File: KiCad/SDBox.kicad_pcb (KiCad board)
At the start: 2 copper layers, 52.5 x 59 mm, 18 parts, among them J1 DB25_Male, J2 Micro_SD_Card_Socket, U1 Rapberry_Pi_Pico_2W, U2 SN74CB3T16210

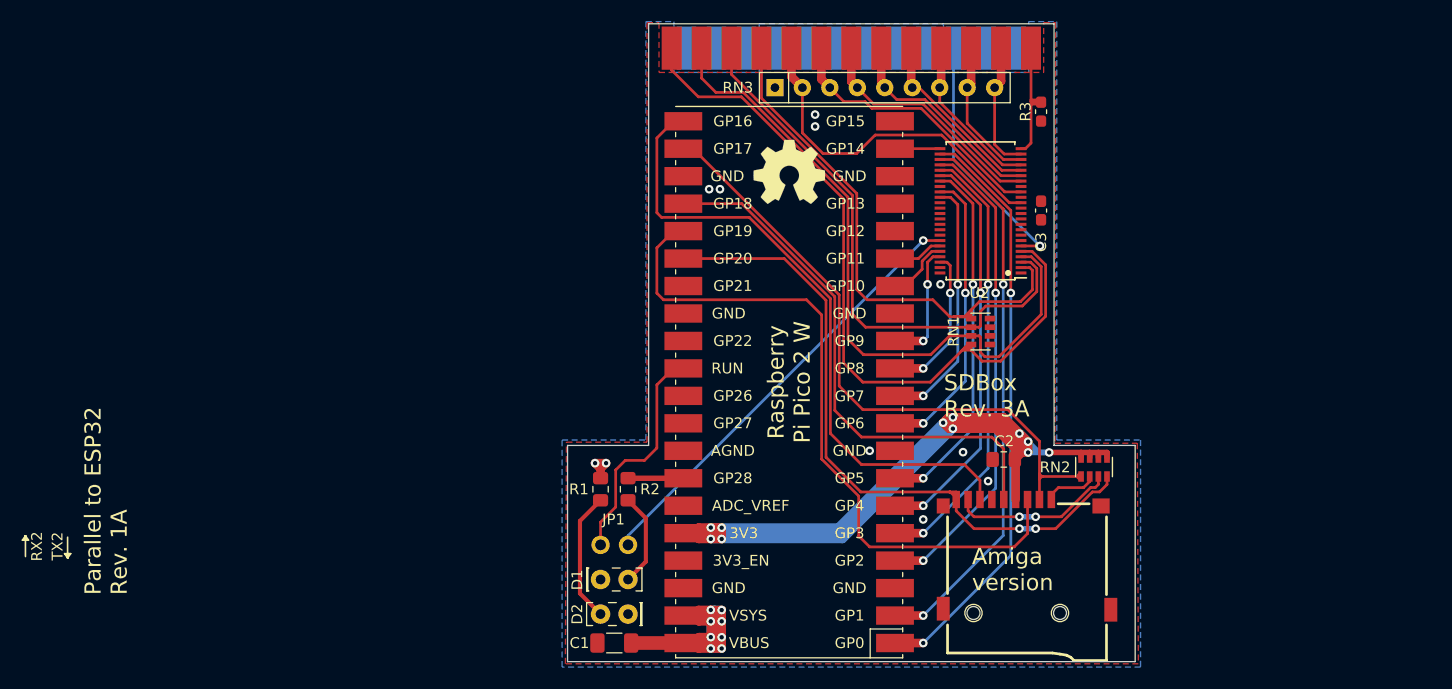
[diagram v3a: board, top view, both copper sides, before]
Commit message: Change board to four layer
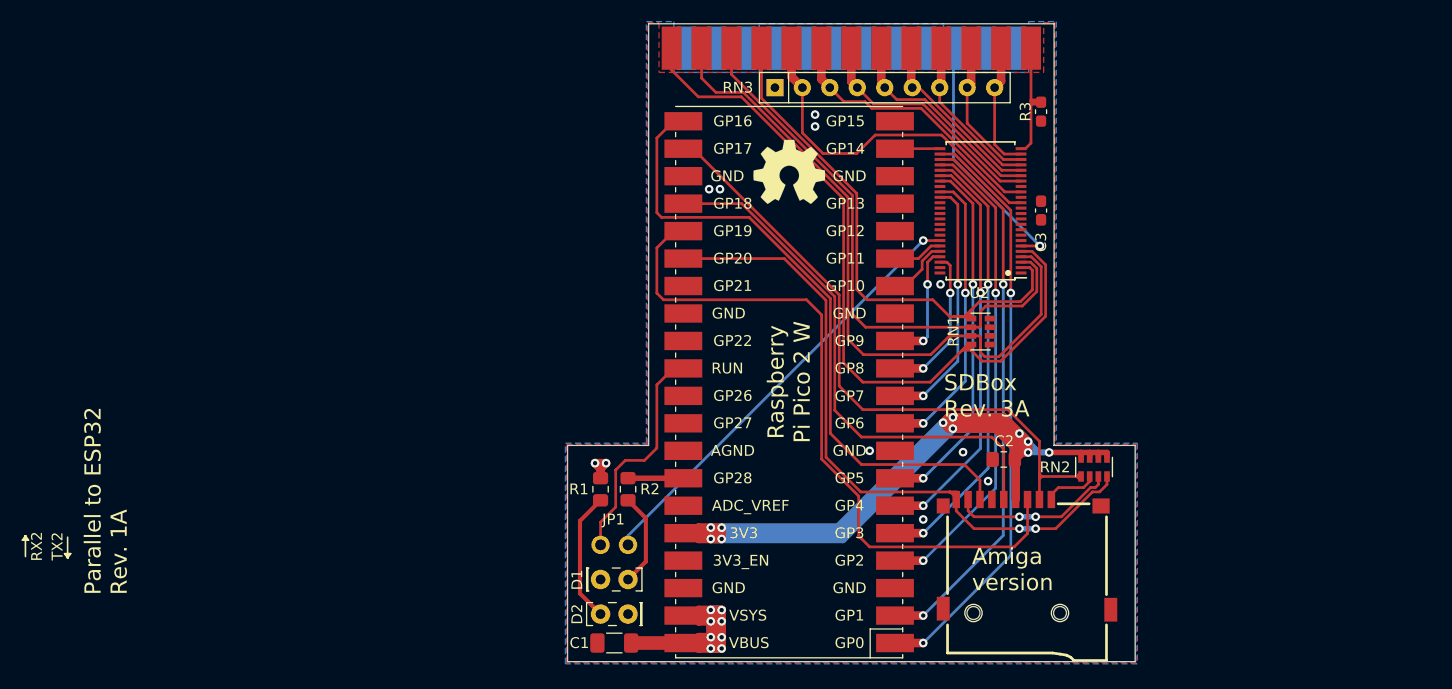
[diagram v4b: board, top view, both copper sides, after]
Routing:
- net VCC: track 49.1 -> 48.2 mm
- net GND: vias 7 -> 9
- net (no net): vias 2 -> 0
- added copper zone on GND, net GND
- added copper zone on VCC, net VCC
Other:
- copper layers 2 -> 4
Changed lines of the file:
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@@
   (general
     (thickness 1.6)
-    (drawings 39)
-    (tracks 481)
+    (drawings 34)
+    (tracks 479)
     (zones 0)
     (modules 18)
@@
   (layers
     (0 F.Cu signal)
+    (1 GND power)
+    (2 VCC power)
     (31 B.Cu signal)
     (32 B.Adhes user)
@@
     (arrow2b (pts (xy 131.45 153.5) (xy 132.576504 152.913579)))
   )
-  (dimension 7 (width 0.15) (layer Dwgs.User)
-    (gr_text "7.000 mm" (at 110.65 127.5 270) (layer Dwgs.User)
-      (effects (font (size 1 1) (thickness 0.15)))
-    )
-    (feature1 (pts (xy 166.45 131) (xy 111.363579 131)))
-    (feature2 (pts (xy 166.45 124) (xy 111.363579 124)))
-    (crossbar (pts (xy 111.95 124) (xy 111.95 131)))
-    (arrow1a (pts (xy 111.95 131) (xy 111.363579 129.873496)))
-    (arrow1b (pts (xy 111.95 131) (xy 112.536421 129.873496)))
-    (arrow2a (pts (xy 111.95 124) (xy 111.363579 125.126504)))
-    (arrow2b (pts (xy 111.95 124) (xy 112.536421 125.126504)))
-  )
-  (dimension 46 (width 0.15) (layer Dwgs.User)
-    (gr_text "46.000 mm" (at 177.75 108 270) (layer Dwgs.User)
-      (effects (font (size 1 1) (thickness 0.15)))
-    )
-    (feature1 (pts (xy 166.45 131) (xy 177.036421 131)))
-    (feature2 (pts (xy 166.45 85) (xy 177.036421 85)))
-    (crossbar (pts (xy 176.45 85) (xy 176.45 131)))
-    (arrow1a (pts (xy 176.45 131) (xy 175.863579 129.873496)))
-    (arrow1b (pts (xy 176.45 131) (xy 177.036421 129.873496)))
-    (arrow2a (pts (xy 176.45 85) (xy 175.863579 86.126504)))
-    (arrow2b (pts (xy 176.45 85) (xy 177.036421 86.126504)))
-  )
   (gr_line (start 121.45 144) (end 173.95 144) (layer Edge.Cuts) (width 0.05))
   (gr_line (start 121.45 124) (end 121.45 144) (layer Edge.Cuts) (width 0.05))
@@
   (gr_line (start 173.95 124) (end 173.95 144) (layer Edge.Cuts) (width 0.05))
   (gr_line (start 166.45 124) (end 173.95 124) (layer Edge.Cuts) (width 0.05))
-  (dimension 52.5 (width 0.15) (layer Dwgs.User)
-    (gr_text "52.500 mm" (at 147.7 145.05) (layer Dwgs.User)
-      (effects (font (size 1 1) (thickness 0.15)))
-    )
-    (feature1 (pts (xy 173.95 124) (xy 173.95 144.336421)))
-    (feature2 (pts (xy 121.45 124) (xy 121.45 144.336421)))
-    (crossbar (pts (xy 121.45 143.75) (xy 173.95 143.75)))
-    (arrow1a (pts (xy 173.95 143.75) (xy 172.823496 144.336421)))
-    (arrow1b (pts (xy 173.95 143.75) (xy 172.823496 143.163579)))
-    (arrow2a (pts (xy 121.45 143.75) (xy 122.576504 144.336421)))
-    (arrow2b (pts (xy 121.45 143.75) (xy 122.576504 143.163579)))
-  )
-  (dimension 7.5 (width 0.15) (layer Dwgs.User)
-    (gr_text "7.500 mm" (at 125.2 125.3) (layer Dwgs.User)
-      (effects (font (size 1 1) (thickness 0.15)))
-    )
-    (feature1 (pts (xy 128.95 124) (xy 128.95 124.586421)))
-    (feature2 (pts (xy 121.45 124) (xy 121.45 124.586421)))
-    (crossbar (pts (xy 121.45 124) (xy 128.95 124)))
-    (arrow1a (pts (xy 128.95 124) (xy 127.823496 124.586421)))
-    (arrow1b (pts (xy 128.95 124) (xy 127.823496 123.413579)))
-    (arrow2a (pts (xy 121.45 124) (xy 122.576504 124.586421)))
-    (arrow2b (pts (xy 121.45 124) (xy 122.576504 123.413579)))
-  )
-  (dimension 39 (width 0.15) (layer Dwgs.User)
-    (gr_text "39.000 mm" (at 171.5 104.5 270) (layer Dwgs.User)
-      (effects (font (size 1 1) (thickness 0.15)))
-    )
-    (feature1 (pts (xy 166.45 124) (xy 170.786421 124)))
-    (feature2 (pts (xy 166.45 85) (xy 170.786421 85)))
-    (crossbar (pts (xy 170.2 85) (xy 170.2 124)))
-    (arrow1a (pts (xy 170.2 124) (xy 169.613579 122.873496)))
-    (arrow1b (pts (xy 170.2 124) (xy 170.786421 122.873496)))
-    (arrow2a (pts (xy 170.2 85) (xy 169.613579 86.126504)))
-    (arrow2b (pts (xy 170.2 85) (xy 170.786421 86.126504)))
-  )
   (gr_text "Amiga\nversion" (at 158.8585 135.4825) (layer F.SilkS)
     (effects (font (size 1.5 1.5) (thickness 0.2)) (justify left))
@@
   (gr_line (start 166.45 85) (end 166.45 124) (layer Edge.Cuts) (width 0.05))
   (gr_line (start 128.95 85) (end 166.45 85) (layer Edge.Cuts) (width 0.05))
+  (via (at 144.35 93.4) (size 0.8) (drill 0.4) (layers F.Cu B.Cu) (net 1))
+  (via (at 144.35 94.5) (size 0.8) (drill 0.4) (layers F.Cu B.Cu) (net 1))
   (via (at 154.35 130.847) (size 0.8) (drill 0.4) (layers F.Cu B.Cu) (net 1))
   (via (at 158.033 124.624) (size 0.8) (drill 0.4) (layers F.Cu B.Cu) (net 1))
@@
   (via (at 135.55 100.3) (size 0.8) (drill 0.4) (layers F.Cu B.Cu) (net 1))
   (via (at 134.55 100.3) (size 0.8) (drill 0.4) (layers F.Cu B.Cu) (net 1))
-  (via (at 144.35 93.4) (size 0.8) (drill 0.4) (layers F.Cu B.Cu) (net 0))
-  (via (at 144.35 94.5) (size 0.8) (drill 0.4) (layers F.Cu B.Cu) (net 0))
   (via (at 165.15 105.55) (size 0.8) (drill 0.4) (layers F.Cu B.Cu) (net 2))
   (segment (start 165.15 105.55) (end 163.4 105.55) (width 0.254) (layer F.Cu) (net 2))
@@
   (segment (start 135.7064 139.229) (end 135.7064 140.2704) (width 0.8) (layer F.Cu) (net 50))
   (segment (start 134.7004 140.2704) (end 134.7 140.27) (width 0.8) (layer F.Cu) (net 50))
-  (segment (start 135.7064 140.2704) (end 134.7004 140.2704) (width 0.8) (layer F.Cu) (net 50))
   (segment (start 133.6024 141.7346) (end 133.06 142.277) (width 0.8) (layer F.Cu) (net 50))
   (segment (start 134.7 141.7346) (end 133.6024 141.7346) (width 0.8) (layer F.Cu) (net 50))
@@
   (segment (start 135.7064 141.7436) (end 135.7064 140.2704) (width 0.8) (layer F.Cu) (net 50))
   (segment (start 134.7 141.7346) (end 134.7 140.27) (width 0.8) (layer F.Cu) (net 50))
-  (segment (start 135.173 142.277) (end 135.7064 141.7436) (width 0.8) (layer F.Cu) (net 50))
   (segment (start 133.06 142.277) (end 135.173 142.277) (width 0.8) (layer F.Cu) (net 50))
   (segment (start 135.706 142.7846) (end 135.7064 142.785) (width 0.8) (layer F.Cu) (net 50))
@@
   (segment (start 134.7 141.7346) (end 134.7 140.27) (width 0.8) (layer B.Cu) (net 50))
   (segment (start 134.7 140.27) (end 134.7 139.22) (width 0.8) (layer B.Cu) (net 50))
-  (segment (start 135.6974 139.22) (end 135.7064 139.229) (width 0.8) (layer B.Cu) (net 50))
   (segment (start 135.7064 139.229) (end 135.7064 140.2704) (width 0.8) (layer B.Cu) (net 50))
   (segment (start 135.7064 140.2704) (end 135.7064 141.7436) (width 0.8) (layer B.Cu) (net 50))
@@
   (segment (start 134.7004 142.785) (end 134.7 142.7846) (width 0.8) (layer B.Cu) (net 50))
   (segment (start 135.1984 142.785) (end 134.7004 142.785) (width 0.8) (layer B.Cu) (net 50))
-  (segment (start 135.037 139.22) (end 135.6974 139.22) (width 0.8) (layer B.Cu) (net 50))
-  (segment (start 134.7 139.22) (end 135.037 139.22) (width 0.8) (layer B.Cu) (net 50))
   (segment (start 135.1984 142.785) (end 135.1984 139.3814) (width 0.8) (layer B.Cu) (net 50))
-  (segment (start 135.1984 139.3814) (end 135.037 139.22) (width 0.8) (layer B.Cu) (net 50))
   (segment (start 135.7064 142.785) (end 135.1984 142.785) (width 0.8) (layer B.Cu) (net 50))
   (segment (start 133.06 142.277) (end 127.3375 142.277) (width 1.27) (layer F.Cu) (net 50))
@@
   (segment (start 124.505 126.148) (end 123.997 125.64) (width 0.8) (layer F.Cu) (net 50))
   (segment (start 123.997 125.64) (end 125.013 125.64) (width 0.8) (layer F.Cu) (net 50))
+  (segment (start 135.6974 139.22) (end 135.7064 139.229) (width 0.8) (layer B.Cu) (net 50))
+  (segment (start 134.7 139.22) (end 135.6974 139.22) (width 0.8) (layer B.Cu) (net 50))
+  (segment (start 135.6974 139.22) (end 135.7064 139.229) (width 0.8) (layer F.Cu) (net 50))
+  (segment (start 134.7 139.22) (end 135.6974 139.22) (width 0.8) (layer F.Cu) (net 50))
   (segment (start 125.902 126.275) (end 125.902 129.704) (width 0.254) (layer F.Cu) (net 55))
   (segment (start 129.712 124.243) (end 128.569 125.386) (width 0.254) (layer F.Cu) (net 55))
@@
     (polygon
       (pts
-        (xy 166.55 123.8) (xy 174.15 123.8) (xy 174.25 144.2) (xy 121.25 144.2) (xy 121.35 123.7)
-        (xy 128.8 123.7) (xy 128.8 84.9) (xy 129.91 84.9) (xy 129.91 89.5) (xy 165.49 89.5)
-        (xy 165.49 84.9) (xy 166.6 84.9)
+        (xy 166.55 123.9) (xy 174.05 123.9) (xy 174.05 144.1) (xy 121.35 144.1) (xy 121.35 123.9)
+        (xy 128.85 123.9) (xy 128.85 84.9) (xy 129.91 84.9) (xy 129.91 89.5) (xy 165.49 89.5)
+        (xy 165.49 84.9) (xy 166.55 84.9)
       )
     )
@@
     (polygon
       (pts
-        (xy 120.95 123.5) (xy 128.7 123.5) (xy 128.7 84.8) (xy 131.29 84.8) (xy 131.29 89.5)
+        (xy 121.25 123.8) (xy 128.75 123.8) (xy 128.75 84.8) (xy 131.29 84.8) (xy 131.29 89.5)
         (xy 139.18 89.5) (xy 139.18 87.3) (xy 139.18 85) (xy 156.22 85) (xy 156.22 89.5)
-        (xy 164.11 89.5) (xy 164.1 84.8) (xy 166.7 84.8) (xy 166.7 123.5) (xy 174.45 123.5)
-        (xy 174.45 144.5) (xy 120.95 144.5)
+        (xy 164.11 89.5) (xy 164.1 84.8) (xy 166.65 84.8) (xy 166.65 123.8) (xy 174.15 123.8)
+        (xy 174.15 144.2) (xy 121.25 144.2)
       )
     )
@@
       )
     )
+  )
+  (zone (net 1) (net_name GND) (layer GND) (hatch edge 0.508)
+    (connect_pads (clearance 0.1524))
+    (min_thickness 0.1524)
+    (fill yes (arc_segments 32) (thermal_gap 0.1524) (thermal_bridge_width 0.508))
+    (polygon
+      (pts
+        (xy 121.15 123.7) (xy 128.65 123.7) (xy 128.65 84.7) (xy 166.75 84.7) (xy 166.75 123.7)
+        (xy 174.25 123.7) (xy 174.25 144.3) (xy 121.15 144.3)
+      )
+    )
+  )
+  (zone (net 50) (net_name VCC) (layer VCC) (hatch edge 0.508)
+    (connect_pads (clearance 0.1524))
+    (min_thickness 0.1524)
+    (fill yes (arc_segments 32) (thermal_gap 0.1524) (thermal_bridge_width 0.508))
+    (polygon
+      (pts
+        (xy 121.05 123.6) (xy 128.55 123.6) (xy 128.55 84.6) (xy 166.85 84.6) (xy 166.85 123.6)
+        (xy 174.35 123.6) (xy 174.35 144.4) (xy 121.05 144.4)
+      )
+    )

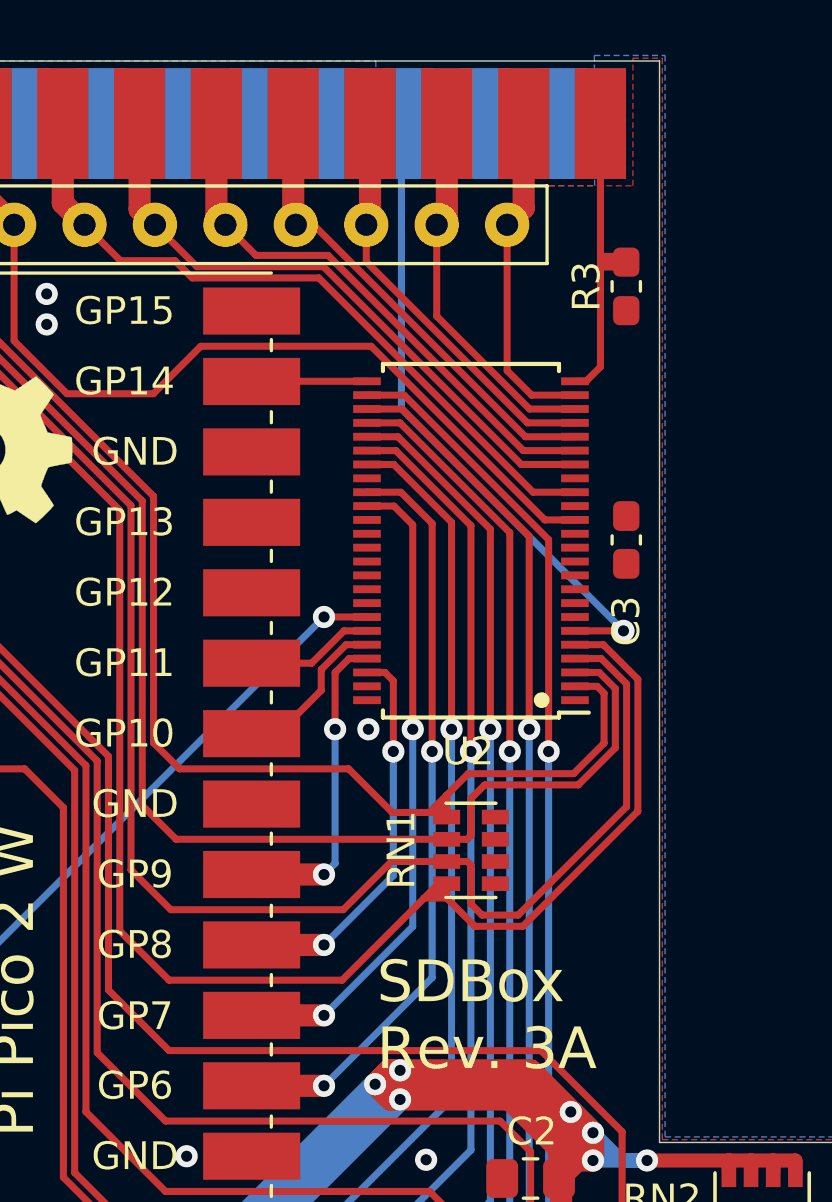
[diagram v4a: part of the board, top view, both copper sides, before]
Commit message: Change U2 SN74CB3T16210 to SN74CBT16210 and add diode D3 and resistor R4 to drop VCC to 4.3V power supply for U2
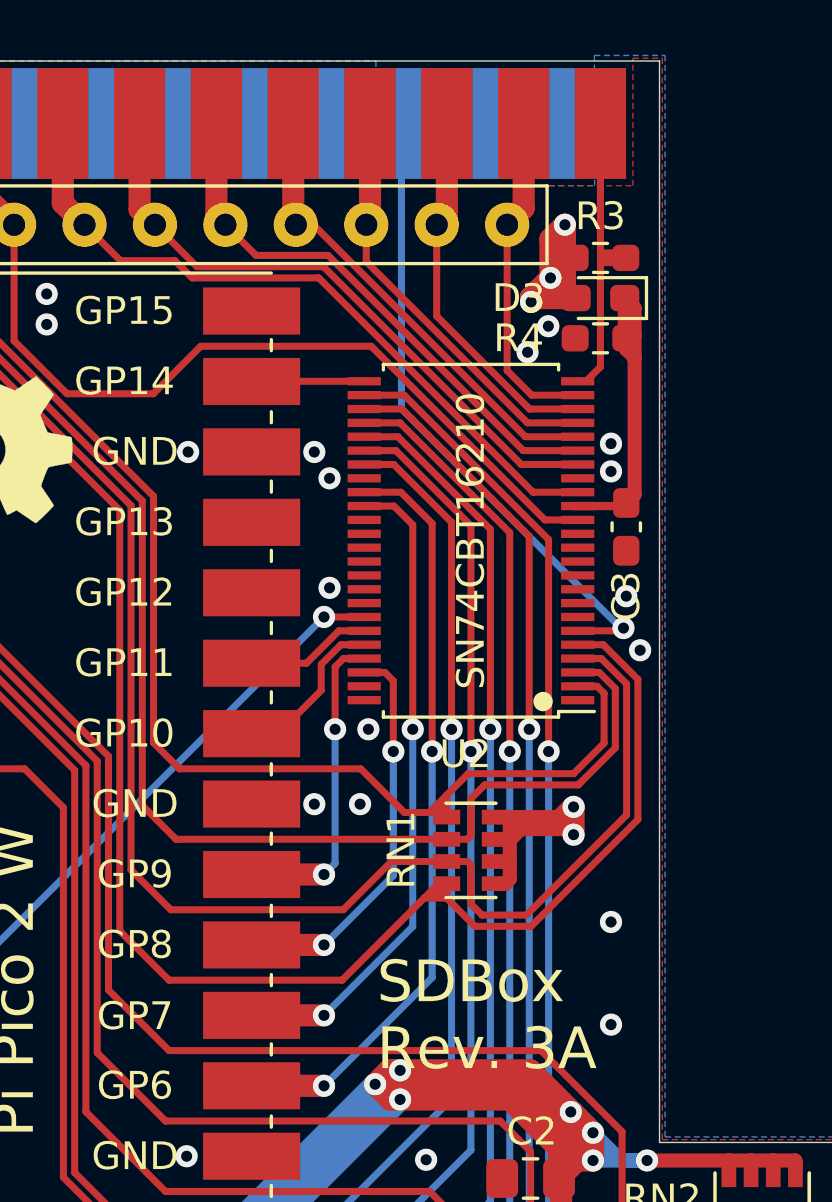
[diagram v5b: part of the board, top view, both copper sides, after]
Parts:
- added D3: D_Small, Diode_SMD:D_0603_1608Metric_Pad1.05x0.95mm_HandSolder, F.Cu at (164.3, 93.5)
- added R4: 2.9k, Resistor_SMD:R_0603_1608Metric_Pad0.98x0.95mm_HandSolder, F.Cu at (164.3, 95.0)
- R3: footprint Resistor_SMD:R_0603_1608Metric_Pad1.05x0.95mm_HandSolder -> Resistor_SMD:R_0603_1608Metric_Pad0.98x0.95mm_HandSolder
- U2: value SN74CB3T16210 -> SN74CBT16210
- moved R3 1.39 mm to (164.3, 92.1), turned to 0 degrees
- moved C3 0.47 mm to (165.2, 101.8)
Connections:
- C3 pad 1: 3V3 -> /4V3
- U2 pad 10: Net-(U2-Pad10) -> GND
- U2 pad 11: Net-(U2-Pad11) -> GND
- U2 pad 12: Net-(U2-Pad12) -> GND
- U2 pad 15: 3V3 -> /4V3
- U2 pad 7: Net-(U2-Pad7) -> GND
- U2 pad 9: Net-(U2-Pad9) -> GND
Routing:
- net VCC: track 48.2 -> 75.2 mm, vias 10 -> 15
- net /4V3: track 0.00 -> 12.3 mm
- net ACK: track 50.3 -> 49.3 mm
- net GND: vias 9 -> 23
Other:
- board text added: "SN74CBT16210"
